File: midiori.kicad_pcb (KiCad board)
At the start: 2 copper layers, 141 x 150 mm, 83 parts, among them J1 midiori-rescue_x68000_expansi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, J2 Conn_ARM_JTAG_SWD_10, J3 AudioJack3, J4 Mini-DIN-5, J5 AudioJack3, J6 AudioJack3, J7 Conn_01x06, J8 AudioJack3, J9 Mini-DIN-5, U1 74LCX07, U10 ICE40HX1K-VQ100, U11 AP2205K-3.3, U12 AK4432, U13 TL074, U14 AP2205K-3.3, U15 TL072, U16 74LCX07, U17 PC817, U18 SN74LVC245APW, U2 AT25SF081-SSHD-X, U3 AP2127K-1.2, U4 SN74LVC245APW, U5 SN74LVC245APW, U6 SN74LVC245APW, U7 SN74LVC245APW, U8 SN74LVC245APW, U9 SN74LVC245APW, X1 16MHz, X2 24.576MHz

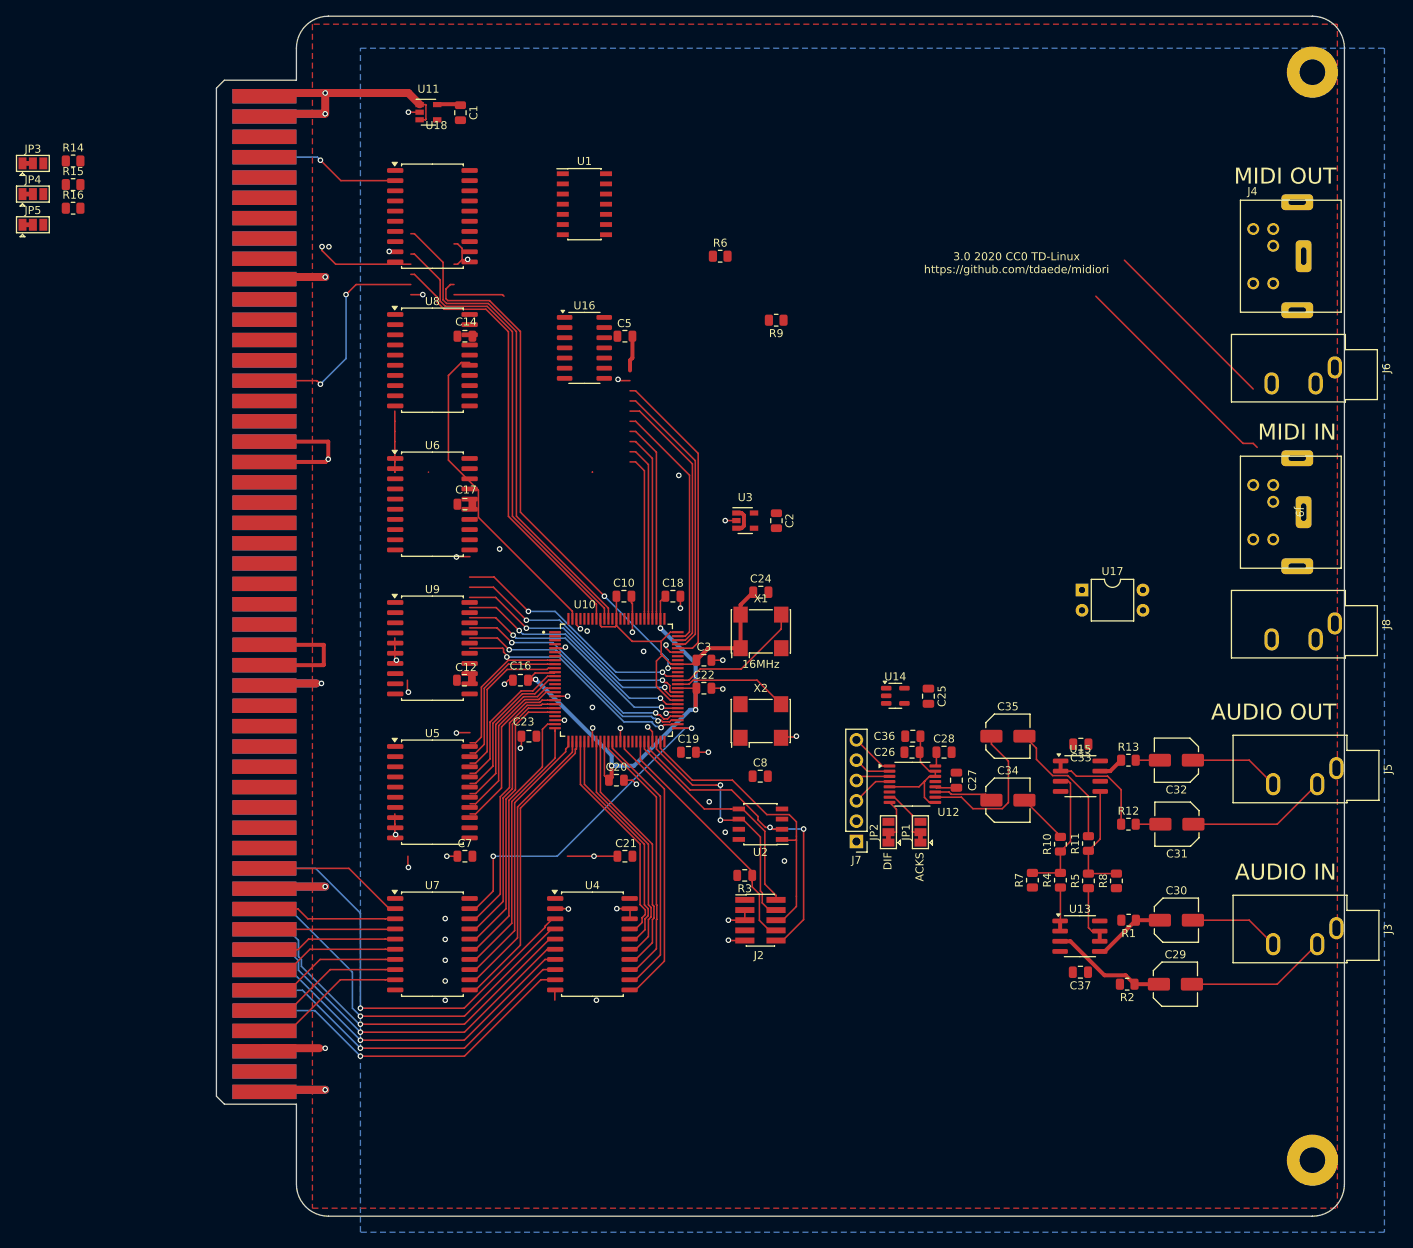
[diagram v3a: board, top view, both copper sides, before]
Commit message: swap optos
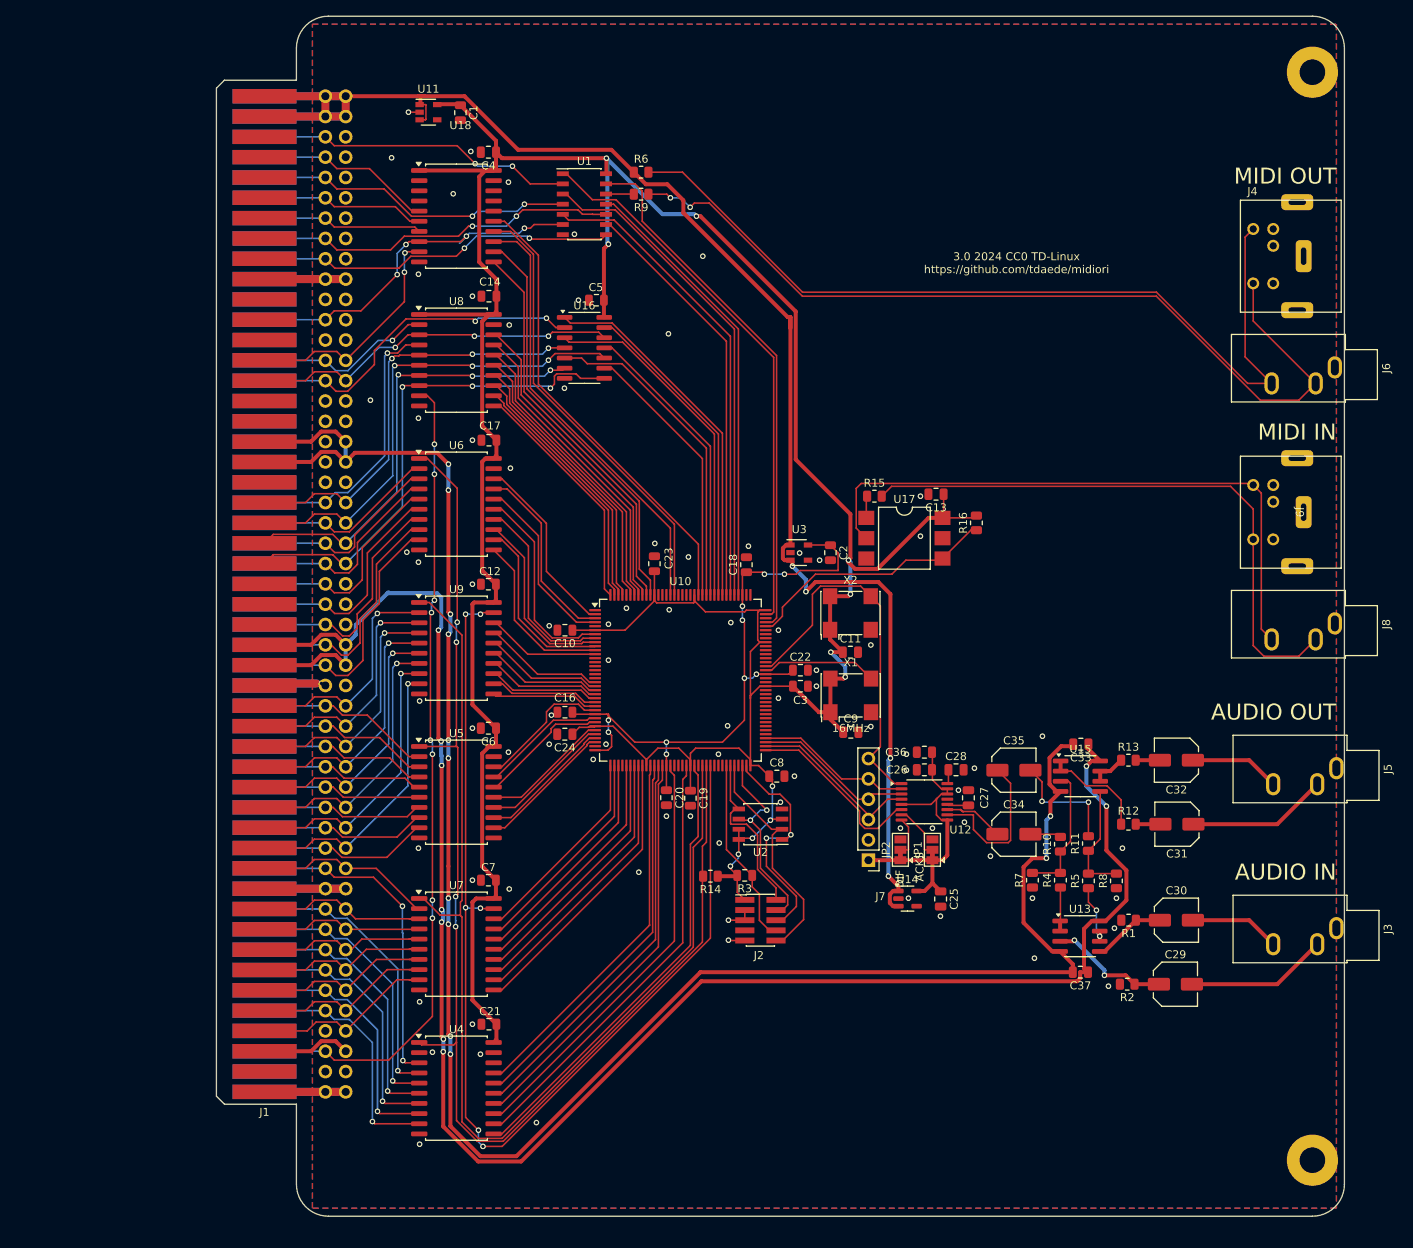
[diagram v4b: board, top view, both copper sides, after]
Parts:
- removed JP3, JP4, JP5: Jumper_3_Bridged12, Jumper:SolderJumper-3_P1.3mm_Bridged12_Pad1.0x1.5mm
- added C11: 0.1uF, Capacitor_SMD:C_0805_2012Metric, F.Cu at (123.2, 118.5)
- added C13: 0.1uF, Capacitor_SMD:C_0805_2012Metric, F.Cu at (133.9, 98.8)
- added C4: 0.1uF, Capacitor_SMD:C_0805_2012Metric, F.Cu at (78.0, 56.0)
- added C6: 0.1uF, Capacitor_SMD:C_0805_2012Metric, F.Cu at (78.0, 128.0)
- added C9: 0.1uF, Capacitor_SMD:C_0805_2012Metric, F.Cu at (123.3, 128.5)
- J1: footprint x68k:x68000_expansion -> x68k:x68000_expansion_vias
- U10: value ICE40HX1K-VQ100 -> ICE40HX1K-TQ144; footprint ICE40HX1K-VQ100:QFP50P1600X1600X120-100N -> Package_QFP:TQFP-144_20x20mm_P0.5mm
- U17: value PC817 -> H11L1; footprint Package_DIP:DIP-4_W7.62mm -> Package_DIP:SMDIP-6_W9.53mm
- moved R14 119.7 mm to (105.8, 146.5), turned to 180 degrees
- moved R16 119.6 mm to (139.0, 102.3), turned to 90 degrees
- moved R15 107.5 mm to (126.2, 99.0)
- moved C24 30.3 mm to (87.5, 128.8), turned to 180 degrees
- moved C21 27.0 mm to (78.1, 165.0)
- moved C23 26.7 mm to (98.8, 107.4), turned to 90 degrees
- moved U14 25.4 mm to (130.4, 149.3)
- moved C25 25.4 mm to (134.5, 149.3)
- moved U4 24.8 mm to (74.0, 173.0)
- moved U17 23.1 mm to (130.0, 104.2)
- moved R9 23.1 mm to (97.1, 61.2)
- moved X2 17.5 mm to (123.2, 113.6)
- moved R6 14.4 mm to (97.1, 58.5)
- moved X1 13.8 mm to (123.3, 123.9)
- moved C3 12.5 mm to (117.0, 122.8)
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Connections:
- J1 pad A29: unconnected-(J1-PadA29) -> /UDS
- U1 pad 1: /irq2 -> /bgack
- U1 pad 10: /BR -> /IRQ4
- U1 pad 11: /br -> /irq4
- U1 pad 12: /UDS -> Net-(R9-Pad2)
- U1 pad 13: /uds_lds_drv -> /midi_out
- U1 pad 2: /IRQ2 -> /BGACK
- U1 pad 3: /irq4 -> /br
- U1 pad 4: /IRQ4 -> /BR
- U1 pad 5: /dtack_drv -> /exown_drv
- U1 pad 6: /DTACK -> /EXOWN
- U1 pad 8: Net-(R9-Pad2) -> /IRQ2
- U1 pad 9: /midi_out -> /irq2
- U10 pad 1: /lds -> unconnected-(U10D-IOL_1A-Pad1)
- U10 pad 10: /ab13 -> /a17
- U10 pad 100: /rw -> +3V3
- U10 pad 11: +1V2 -> /a16
- U10 pad 12: /ab12 -> /db15
- U10 pad 13: /ab11 -> GND
- U10 pad 14: +3V3 -> GND
- U10 pad 15: /ab10 -> unconnected-(U10A-NC-Pad15)
- U10 pad 16: /ab9 -> unconnected-(U10A-NC-Pad16)
- U10 pad 17: GND -> unconnected-(U10A-NC-Pad17)
- U10 pad 18: /ab8 -> unconnected-(U10A-NC-Pad18)
- U10 pad 19: /d7 -> /db14
- U10 pad 2: /as -> /a23
- U10 pad 20: /d6 -> /db13
- U10 pad 21: /d5 -> /db12
- U10 pad 22: +3V3 -> /db11
- U10 pad 23: GND -> /db10
- U10 pad 24: /d4 -> /db9
- U10 pad 25: /d3 -> /db8
- U10 pad 26: /d2 -> /ab15
- U10 pad 27: /d1 -> +1V2
- U10 pad 28: /d0 -> /ab14
- U10 pad 29: /a7 -> /ab13
- U10 pad 3: /bg -> /a22
- U10 pad 30: /a6 -> +3V3
- U10 pad 31: +3V3 -> /ab12
- U10 pad 32: GND -> /ab11
- U10 pad 33: /a5 -> /ab10
- U10 pad 34: /a4 -> /ab9
- U10 pad 35: +1V2 -> GND
- U10 pad 36: /a3 -> +1V2
- U10 pad 37: /a2 -> /d7
- U10 pad 38: +3V3 -> /d6
- U10 pad 39: GND -> /d5
- U10 pad 4: /midi_in -> /a21
- U10 pad 40: /a1 -> unconnected-(U10B-NC-Pad40)
- U10 pad 41: /rw_drv -> /d4
- U10 pad 42: /as_drv -> /d3
- U10 pad 43: unconnected-(U10-CDONE-Pad43) -> /d2
- U10 pad 44: /reset -> /d1
- U10 pad 45: /si -> /d0
- U10 pad 46: /so -> +3V3
- U10 pad 47: GND -> /a7
- U10 pad 48: /sck -> /a6
- U10 pad 49: /ss -> /a5
- U10 pad 50: +3V3 -> /a4
- U10 pad 51: /xltr_oe -> +1V2
- U10 pad 52: /db8 -> /a3
- U10 pad 53: /db9 -> unconnected-(U10B-NC-Pad53)
- U10 pad 54: /db10 -> unconnected-(U10B-NC-Pad54)
- U10 pad 55: GND -> unconnected-(U10B-NC-Pad55)
- U10 pad 56: /db11 -> /a2
- U10 pad 57: /db12 -> +3V3
- U10 pad 58: +3V3 -> /a1
- U10 pad 59: /db13 -> GND
- U10 pad 60: /db14 -> /data_dir
- U10 pad 61: +1V2 -> /addr_dir
- U10 pad 62: /24.576mhz -> /xltr_oe
- U10 pad 63: /16mhz -> unconnected-(U10C-IOB_42_CBSEL0-Pad63)
- U10 pad 64: /db15 -> unconnected-(U10C-IOB_43_CBSEL1-Pad64)
- U10 pad 65: /bgack -> unconnected-(U10E-CDONE-Pad65)
- U10 pad 66: /midi_out -> /reset
- U10 pad 67: +3V3 -> /si
- U10 pad 68: /br -> /so
- U10 pad 69: /data_dir -> GND
- U10 pad 7: /uds_lds_drv -> /a20
- U10 pad 70: GND -> /sck
- U10 pad 71: /a23 -> /ss
- U10 pad 72: /a22 -> +3V3
- U10 pad 73: /a21 -> /smute
- U10 pad 74: /a20 -> /lrck
- U10 pad 75: +3V3 -> /sdti
- U10 pad 76: unconnected-(U10-VPP_FAST-Pad76) -> /bick
- U10 pad 77: +1V2 -> unconnected-(U10A-NC-Pad77)
- U10 pad 78: /a19 -> unconnected-(U10B-IOR_52-Pad78)
- U10 pad 79: /a18 -> unconnected-(U10B-IOR_53-Pad79)
- U10 pad 8: /ab15 -> /a19
- U10 pad 80: /a17 -> unconnected-(U10B-IOR_54-Pad80)
- U10 pad 81: /a16 -> unconnected-(U10B-IOR_55-Pad81)
- U10 pad 82: /dtack -> unconnected-(U10B-NC-Pad82)
- U10 pad 83: Net-(JP4-C) -> unconnected-(U10C-NC-Pad83)
- U10 pad 84: GND -> unconnected-(U10C-NC-Pad84)
- U10 pad 85: /smute -> unconnected-(U10C-NC-Pad85)
- U10 pad 86: /sdti -> GND
- U10 pad 87: /lrck -> unconnected-(U10B-IOR_56-Pad87)
- U10 pad 88: +3V3 -> unconnected-(U10B-IOR_57-Pad88)
- U10 pad 89: /10m -> +3V3
- U10 pad 9: /ab14 -> /a18
- U10 pad 90: /irq2 -> unconnected-(U10B-IOR_58-Pad90)
- U10 pad 91: /irq4 -> unconnected-(U10B-IOR_59-Pad91)
- U10 pad 92: +3V3 -> +1V2
- U10 pad 93: /dtack_drv -> /16mhz
- U10 pad 94: /iack2 -> /24.576mhz
- U10 pad 95: /iack4 -> unconnected-(U10B-IOR_62-Pad95)
- U10 pad 96: /iddir -> unconnected-(U10B-IOR_63-Pad96)
- U10 pad 97: /exown -> unconnected-(U10B-IOR_64-Pad97)
- U10 pad 98: GND -> unconnected-(U10B-IOR_65-Pad98)
- U10 pad 99: /exreset -> unconnected-(U10B-IOR_66-Pad99)
- U16 pad 1: /exown_drv -> /exreq_drv
- U16 pad 10: /BGACK -> /UDS
- U16 pad 11: /bgack -> /uds_drv
- U16 pad 12: /LDS -> /DTACK
- U16 pad 13: /uds_lds_drv -> /dtack_drv
- U16 pad 2: /EXOWN -> /EXREQ
- U16 pad 3: /exreq_drv -> /rw_drv
- U16 pad 4: /EXREQ -> /RW
- U16 pad 5: /as_drv -> /lds_drv
- U16 pad 6: /AS -> /LDS
- U16 pad 8: /RW -> /AS
- U16 pad 9: /rw_drv -> /as_drv
- U17 pad 3: GND -> unconnected-(U17-Pad3)
- U18 pad 11: GND -> /exreset
- U18 pad 12: GND -> /exown
- U18 pad 13: GND -> /iack2
- U18 pad 14: /exack -> /iack4
- U18 pad 15: /dtack -> /bg
- U18 pad 16: /exown -> unconnected-(U18-B3-Pad16)
- U18 pad 17: /uds -> unconnected-(U18-B2-Pad17)
- U18 pad 18: /bg -> unconnected-(U18-B1-Pad18)
- U18 pad 2: /BG -> unconnected-(U18-A1-Pad2)
- U18 pad 3: /UDS -> unconnected-(U18-A2-Pad3)
- U18 pad 4: /EXOWN -> unconnected-(U18-A3-Pad4)
- U18 pad 5: /DTACK -> /BG
- U18 pad 6: /EXACK -> /IACK4
- U18 pad 7: GND -> /IACK2
- U18 pad 8: GND -> /EXOWN
- U18 pad 9: GND -> /EXRESET
- U8 pad 11: /iddir -> /10m
- U8 pad 12: /iack4 -> /as
- U8 pad 13: /iack2 -> /lds
- U8 pad 14: /as -> /uds
- U8 pad 15: /lds -> /rw
- U8 pad 16: /rw -> /iddir
- U8 pad 17: /exreset -> /dtack
- U8 pad 18: /10m -> /exack
- U8 pad 2: /10MHz -> /EXACK
- U8 pad 3: /EXRESET -> /DTACK
- U8 pad 4: /RW -> /IDDIR
- U8 pad 5: /LDS -> /RW
- U8 pad 6: /AS -> /UDS
- U8 pad 7: /IACK2 -> /LDS
- U8 pad 8: /IACK4 -> /AS
- U8 pad 9: /IDDIR -> /10MHz
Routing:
- net +3V3: track 52.8 -> 437.1 mm, vias 1 -> 12
- net -12V: track 18.3 -> 248.2 mm, vias 1 -> 12
- net +12V: track 17.4 -> 236.0 mm, vias 0 -> 9
- net /addr_dir: track 0.00 -> 159.6 mm, vias 0 -> 4
- net +5V: track 52.2 -> 210.5 mm, vias 2 -> 4
- net /data_dir: track 0.00 -> 136.9 mm
- net /10MHz: track 0.00 -> 103.0 mm, vias 0 -> 8
- net /xltr_oe: track 41.3 -> 135.3 mm, vias 2 -> 6
- net /source: track 22.8 -> 109.9 mm
- net /sink: track 28.0 -> 111.1 mm, vias 0 -> 2
- net Net-(J8-PadR): track 0.00 -> 77.0 mm
- net Net-(J8-PadT): track 0.00 -> 74.4 mm
- net /bgack: track 0.00 -> 68.8 mm
- net GND: track 157.5 -> 92.0 mm, vias 55 -> 83
- net /AS: track 0.00 -> 63.1 mm, vias 0 -> 3
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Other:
- board text added: "3.0 2024 CC0 TD-Linux https://github.com/tdaede/midiori"
- board text removed: "3.0 2020 CC0 TD-Linux https://github.com/tdaede/midiori"

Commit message: crystal swap
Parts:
- moved X2 10.4 mm to (123.2, 124.0)
- moved X1 10.3 mm to (123.2, 113.6)
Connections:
- U10 pad 93: /16mhz -> /24.576mhz
- U10 pad 94: /24.576mhz -> /16mhz
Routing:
- net /24.576mhz: track 47.0 -> 30.9 mm
- net /16mhz: track 14.4 -> 20.1 mm
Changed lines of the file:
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@@
 	(footprint "Oscillator:Oscillator_SMD_SeikoEpson_SG8002CA-4Pin_7.0x5.0mm"
 		(layer "F.Cu")
-		(at 123.29 123.9)
+		(at 123.25 113.6)
 		(descr "SMD Crystal Oscillator Seiko Epson SG-8002CA https://support.epson.biz/td/api/doc_check.php?mode=dl&lang=en&Parts=SG-8002DC, 7.0x5.0mm^2 package")
 		(tags "SMD SMT crystal oscillator")
@@
 			(layers "F.Cu" "F.Paste" "F.Mask")
 			(roundrect_rratio 0.25)
-			(net 174 "/16mhz")
+			(net 102 "/24.576mhz")
 			(pinfunction "IOR_60_GBIN3")
 			(pintype "bidirectional")
@@
 			(layers "F.Cu" "F.Paste" "F.Mask")
 			(roundrect_rratio 0.25)
-			(net 102 "/24.576mhz")
+			(net 174 "/16mhz")
 			(pinfunction "IOR_61_GBIN2")
 			(pintype "bidirectional")
@@
 	(footprint "Oscillator:Oscillator_SMD_SeikoEpson_SG8002CA-4Pin_7.0x5.0mm"
 		(layer "F.Cu")
-		(at 123.25 113.6)
+		(at 123.25 124)
 		(descr "SMD Crystal Oscillator Seiko Epson SG-8002CA https://support.epson.biz/td/api/doc_check.php?mode=dl&lang=en&Parts=SG-8002DC, 7.0x5.0mm^2 package")
 		(tags "SMD SMT crystal oscillator")
@@
 	)
 	(segment
-		(start 126.99 112.7)
-		(end 126.99 130.31)
-		(width 0.2)
-		(layer "F.Cu")
-		(net 102)
-	)
-	(segment
-		(start 124.53 110.24)
-		(end 125.79 111.5)
-		(width 0.2)
-		(layer "F.Cu")
-		(net 102)
-	)
-	(segment
-		(start 119.51 110.24)
-		(end 124.53 110.24)
+		(start 125.79 121.9)
+		(end 127 123.11)
 		(width 0.2)
 		(layer "F.Cu")
@@
 	)
 	(segment
-		(start 118.5 111.25)
-		(end 119.51 110.24)
+		(start 127 130.3)
+		(end 125.5 131.8)
 		(width 0.2)
 		(layer "F.Cu")
@@
 	)
 	(segment
-		(start 126.99 130.31)
-		(end 125.5 131.8)
+		(start 123.82 119.79)
+		(end 114.359999 119.79)
 		(width 0.2)
 		(layer "F.Cu")
@@
 	)
 	(segment
-		(start 118.5 115.12584)
-		(end 118.5 111.25)
+		(start 128.765 134.925)
+		(end 125.5 131.66)
 		(width 0.2)
 		(layer "F.Cu")
@@
 	)
 	(segment
-		(start 125.79 111.5)
-		(end 126.99 112.7)
+		(start 113.399999 120.75)
+		(end 112.6625 120.75)
 		(width 0.2)
 		(layer "F.Cu")
@@
 	)
 	(segment
-		(start 112.6625 120.25)
-		(end 113.37584 120.25)
+		(start 127 123.11)
+		(end 127 130.3)
 		(width 0.2)
 		(layer "F.Cu")
@@
 	)
 	(segment
-		(start 128.765 134.925)
-		(end 125.5 131.66)
+		(start 114.359999 119.79)
+		(end 113.399999 120.75)
 		(width 0.2)
 		(layer "F.Cu")
@@
 	)
 	(segment
-		(start 113.37584 120.25)
-		(end 118.5 115.12584)
+		(start 129.6375 134.925)
+		(end 128.765 134.925)
 		(width 0.2)
 		(layer "F.Cu")
@@
 	)
 	(segment
-		(start 129.6375 134.925)
-		(end 128.765 134.925)
+		(start 125.83 121.8)
+		(end 123.82 119.79)
 		(width 0.2)
 		(layer "F.Cu")
@@
 	)
 	(segment
-		(start 123.82 119.79)
-		(end 114.359999 119.79)
+		(start 124.53 110.24)
+		(end 125.79 111.5)
 		(width 0.2)
 		(layer "F.Cu")
@@
 	)
 	(segment
-		(start 113.399999 120.75)
-		(end 112.6625 120.75)
+		(start 119.51 110.24)
+		(end 124.53 110.24)
 		(width 0.2)
 		(layer "F.Cu")
@@
 	)
 	(segment
-		(start 114.359999 119.79)
-		(end 113.399999 120.75)
+		(start 118.5 111.25)
+		(end 119.51 110.24)
 		(width 0.2)
 		(layer "F.Cu")
@@
 	)
 	(segment
-		(start 125.83 121.8)
-		(end 123.82 119.79)
+		(start 118.5 115.12584)
+		(end 118.5 111.25)
+		(width 0.2)
+		(layer "F.Cu")
+		(net 174)
+	)
+	(segment
+		(start 112.6625 120.25)
+		(end 113.37584 120.25)
+		(width 0.2)
+		(layer "F.Cu")
+		(net 174)
+	)
+	(segment
+		(start 113.37584 120.25)
+		(end 118.5 115.12584)
 		(width 0.2)
 		(layer "F.Cu")

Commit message: missing wire
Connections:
- J8 pad S: GND -> unconnected-(J8-PadS)
- J9 pad 2: GND -> unconnected-(J9-Pad2)
- U10 pad 1: unconnected-(U10D-IOL_1A-Pad1) -> /a23
- U10 pad 10: /a17 -> /a16
- U10 pad 11: /a16 -> /db15
- U10 pad 12: /db15 -> /db14
- U10 pad 19: /db14 -> /db13
- U10 pad 2: /a23 -> /a22
- U10 pad 20: /db13 -> /db12
- U10 pad 21: /db12 -> /db11
- U10 pad 22: /db11 -> /db10
- U10 pad 23: /db10 -> /db9
- U10 pad 24: /db9 -> /db8
- U10 pad 25: /db8 -> /ab15
- U10 pad 26: /ab15 -> /ab14
- U10 pad 28: /ab14 -> /ab13
- U10 pad 29: /ab13 -> /ab12
- U10 pad 3: /a22 -> /a21
- U10 pad 31: /ab12 -> /ab11
- U10 pad 32: /ab11 -> /ab10
- U10 pad 33: /ab10 -> /ab9
- U10 pad 34: /ab9 -> /ab8
- U10 pad 4: /a21 -> /a20
- U10 pad 7: /a20 -> /a19
- U10 pad 8: /a19 -> /a18
- U10 pad 9: /a18 -> /a17
- U18 pad 16: unconnected-(U18-B3-Pad16) -> GND
- U18 pad 17: unconnected-(U18-B2-Pad17) -> GND
- U18 pad 18: unconnected-(U18-B1-Pad18) -> GND
- U18 pad 2: unconnected-(U18-A1-Pad2) -> GND
- U18 pad 3: unconnected-(U18-A2-Pad3) -> GND
- U18 pad 4: unconnected-(U18-A3-Pad4) -> GND
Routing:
- net /ab8: track 0.00 -> 17.8 mm
- net /a20: track 25.3 -> 21.9 mm
- net /ab12: track 16.2 -> 18.7 mm
- net /d7: track 25.8 -> 28.0 mm
- net /ab14: track 15.7 -> 17.9 mm
- net /a7: track 47.2 -> 49.1 mm
- net /d6: track 27.3 -> 29.2 mm
- net /as_drv: track 34.0 -> 35.8 mm
- net /d5: track 28.8 -> 30.4 mm
- net /a6: track 48.6 -> 50.2 mm
- net /sink: track 111.1 -> 112.6 mm
- net /a5: track 50.1 -> 51.4 mm
- net /d4: track 30.4 -> 31.7 mm
- net /db14: track 15.2 -> 14.0 mm
- net /ab13: track 16.3 -> 17.5 mm
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
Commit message: drc fixes
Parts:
- added svg2mod: G***, x68k:midiori_logo, F.Cu at (141.0, 52.5)
- H1, H2: value MountingHole -> MountingHole_Pad
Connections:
- H1 pad 1: (no net) -> GND
- H2 pad 1: (no net) -> GND
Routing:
- net unconnected-(J1-PadA48): track 0.00 -> 11.1 mm
- net unconnected-(J1-PadA47)_1: track 0.00 -> 11.1 mm
- net unconnected-(J1-PadA45): track 0.00 -> 11.1 mm
- net unconnected-(J1-PadA43): track 0.00 -> 11.1 mm
- net unconnected-(J1-PadA42): track 0.00 -> 11.1 mm
- net unconnected-(J1-PadA39): track 0.00 -> 11.1 mm
- net unconnected-(J1-PadA31): track 0.00 -> 11.1 mm
- net unconnected-(J1-FC2-PadA26)_1: track 0.00 -> 11.1 mm
- net unconnected-(J1-FC0-PadA24)_1: track 0.00 -> 11.1 mm
- net unconnected-(J1-PadA46): track 0.00 -> 11.1 mm
- net unconnected-(J1-PadA40)_1: track 0.00 -> 11.1 mm
- net unconnected-(J1-PadA38)_1: track 0.00 -> 11.1 mm
- net unconnected-(J1-PadA35): track 0.00 -> 11.1 mm
- net unconnected-(J1-PadA34): track 0.00 -> 11.1 mm
- net unconnected-(J1-FC1-PadA25)_1: track 0.00 -> 11.1 mm
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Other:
- board text added: "+pcm"
